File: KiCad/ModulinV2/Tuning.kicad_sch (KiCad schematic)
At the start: 35 parts, among them IC51 TL074HIDR

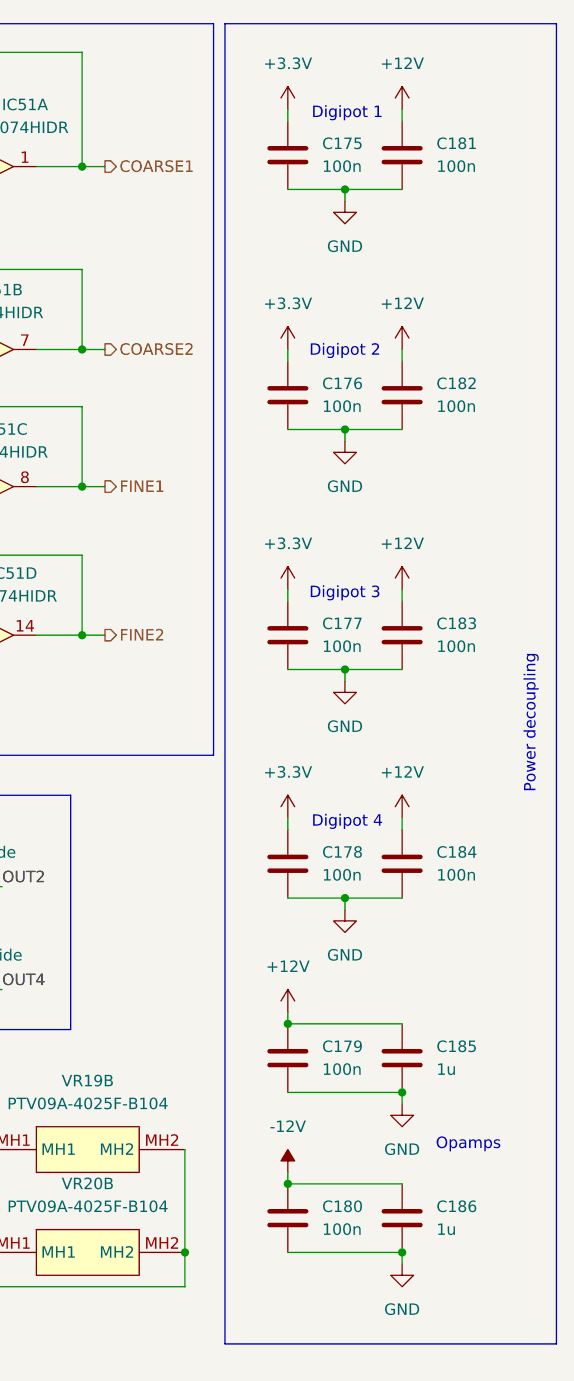
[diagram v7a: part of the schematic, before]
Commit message: Layed out Interface and PWR components and started with MCU layout
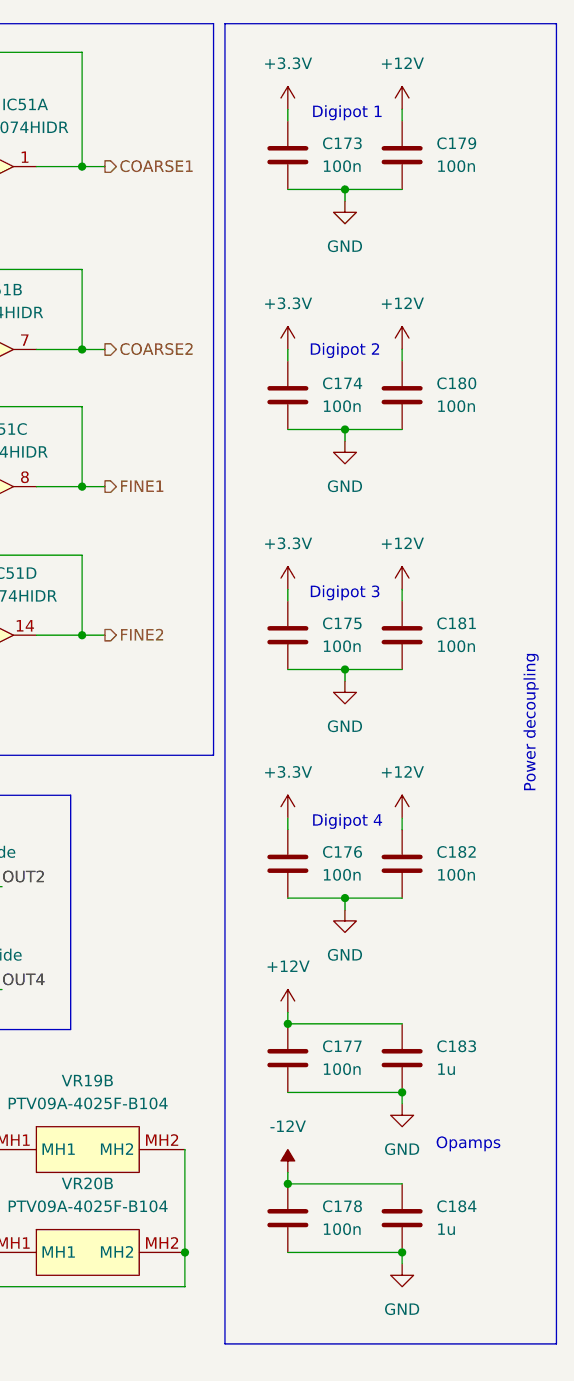
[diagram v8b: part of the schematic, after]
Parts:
- renumbered C175 to C173, C176 to C174, C177 to C175, C178 to C176, C179 to C177, C180 to C178, C181 to C179, C182 to C180, C183 to C181, C184 to C182, C185 to C183, C186 to C184
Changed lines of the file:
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@@
 		(dnp no)
 		(fields_autoplaced yes)
-		(property "Reference" "C176"
+		(property "Reference" "C174"
 			(at 240.03 55.8799 0)
 			(effects
@@
 			(project "ModulinV2"
 				(path "/c6b34a57-3941-4b56-8b80-1848c7f41082/e9498aae-6574-4e4e-b792-2c2c867ca344"
-					(reference "C176")
+					(reference "C174")
 					(unit 1)
 				)
@@
 		(dnp no)
 		(fields_autoplaced yes)
-		(property "Reference" "C181"
+		(property "Reference" "C179"
 			(at 252.73 29.2099 0)
 			(effects
@@
 			(project "ModulinV2"
 				(path "/c6b34a57-3941-4b56-8b80-1848c7f41082/e9498aae-6574-4e4e-b792-2c2c867ca344"
-					(reference "C181")
+					(reference "C179")
 					(unit 1)
 				)
@@
 		(dnp no)
 		(fields_autoplaced yes)
-		(property "Reference" "C184"
+		(property "Reference" "C182"
 			(at 252.73 107.9499 0)
 			(effects
@@
 			(project "ModulinV2"
 				(path "/c6b34a57-3941-4b56-8b80-1848c7f41082/e9498aae-6574-4e4e-b792-2c2c867ca344"
-					(reference "C184")
+					(reference "C182")
 					(unit 1)
 				)
@@
 		(dnp no)
 		(fields_autoplaced yes)
-		(property "Reference" "C183"
+		(property "Reference" "C181"
 			(at 252.73 82.5499 0)
 			(effects
@@
 			(project "ModulinV2"
 				(path "/c6b34a57-3941-4b56-8b80-1848c7f41082/e9498aae-6574-4e4e-b792-2c2c867ca344"
-					(reference "C183")
+					(reference "C181")
 					(unit 1)
 				)
@@
 		(dnp no)
 		(fields_autoplaced yes)
-		(property "Reference" "C186"
+		(property "Reference" "C184"
 			(at 252.73 147.3199 0)
 			(effects
@@
 			(project "ModulinV2"
 				(path "/c6b34a57-3941-4b56-8b80-1848c7f41082/e9498aae-6574-4e4e-b792-2c2c867ca344"
-					(reference "C186")
+					(reference "C184")
 					(unit 1)
 				)
@@
 		(dnp no)
 		(fields_autoplaced yes)
-		(property "Reference" "C179"
+		(property "Reference" "C177"
 			(at 240.03 129.5399 0)
 			(effects
@@
 			(project "ModulinV2"
 				(path "/c6b34a57-3941-4b56-8b80-1848c7f41082/e9498aae-6574-4e4e-b792-2c2c867ca344"
-					(reference "C179")
+					(reference "C177")
 					(unit 1)
 				)
@@
 		(dnp no)
 		(fields_autoplaced yes)
-		(property "Reference" "C185"
+		(property "Reference" "C183"
 			(at 252.73 129.5399 0)
 			(effects
@@
 			(project "ModulinV2"
 				(path "/c6b34a57-3941-4b56-8b80-1848c7f41082/e9498aae-6574-4e4e-b792-2c2c867ca344"
-					(reference "C185")
+					(reference "C183")
 					(unit 1)
 				)
@@
 		(dnp no)
 		(fields_autoplaced yes)
-		(property "Reference" "C180"
+		(property "Reference" "C178"
 			(at 240.03 147.3199 0)
 			(effects
@@
 			(project "ModulinV2"
 				(path "/c6b34a57-3941-4b56-8b80-1848c7f41082/e9498aae-6574-4e4e-b792-2c2c867ca344"
-					(reference "C180")
+					(reference "C178")
 					(unit 1)
 				)
@@
 		(dnp no)
 		(fields_autoplaced yes)
-		(property "Reference" "C182"
+		(property "Reference" "C180"
 			(at 252.73 55.8799 0)
 			(effects
@@
 			(project "ModulinV2"
 				(path "/c6b34a57-3941-4b56-8b80-1848c7f41082/e9498aae-6574-4e4e-b792-2c2c867ca344"
-					(reference "C182")
+					(reference "C180")
 					(unit 1)
 				)
@@
 		(dnp no)
 		(fields_autoplaced yes)
-		(property "Reference" "C177"
+		(property "Reference" "C175"
 			(at 240.03 82.5499 0)
 			(effects
@@
 			(project "ModulinV2"
 				(path "/c6b34a57-3941-4b56-8b80-1848c7f41082/e9498aae-6574-4e4e-b792-2c2c867ca344"
-					(reference "C177")
+					(reference "C175")
 					(unit 1)
 				)
@@
 		(dnp no)
 		(fields_autoplaced yes)
-		(property "Reference" "C178"
+		(property "Reference" "C176"
 			(at 240.03 107.9499 0)
 			(effects
@@
 			(project "ModulinV2"
 				(path "/c6b34a57-3941-4b56-8b80-1848c7f41082/e9498aae-6574-4e4e-b792-2c2c867ca344"
-					(reference "C178")
+					(reference "C176")
 					(unit 1)
 				)
@@
 		(dnp no)
 		(fields_autoplaced yes)
-		(property "Reference" "C175"
+		(property "Reference" "C173"
 			(at 240.03 29.2099 0)
 			(effects
@@
 			(project "ModulinV2"
 				(path "/c6b34a57-3941-4b56-8b80-1848c7f41082/e9498aae-6574-4e4e-b792-2c2c867ca344"
-					(reference "C175")
+					(reference "C173")
 					(unit 1)
 				)
